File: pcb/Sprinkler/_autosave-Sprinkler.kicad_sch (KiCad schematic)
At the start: 6 parts, among them SW1 SW_Push_Open, U1 DHT11, U2 DS3231MZ

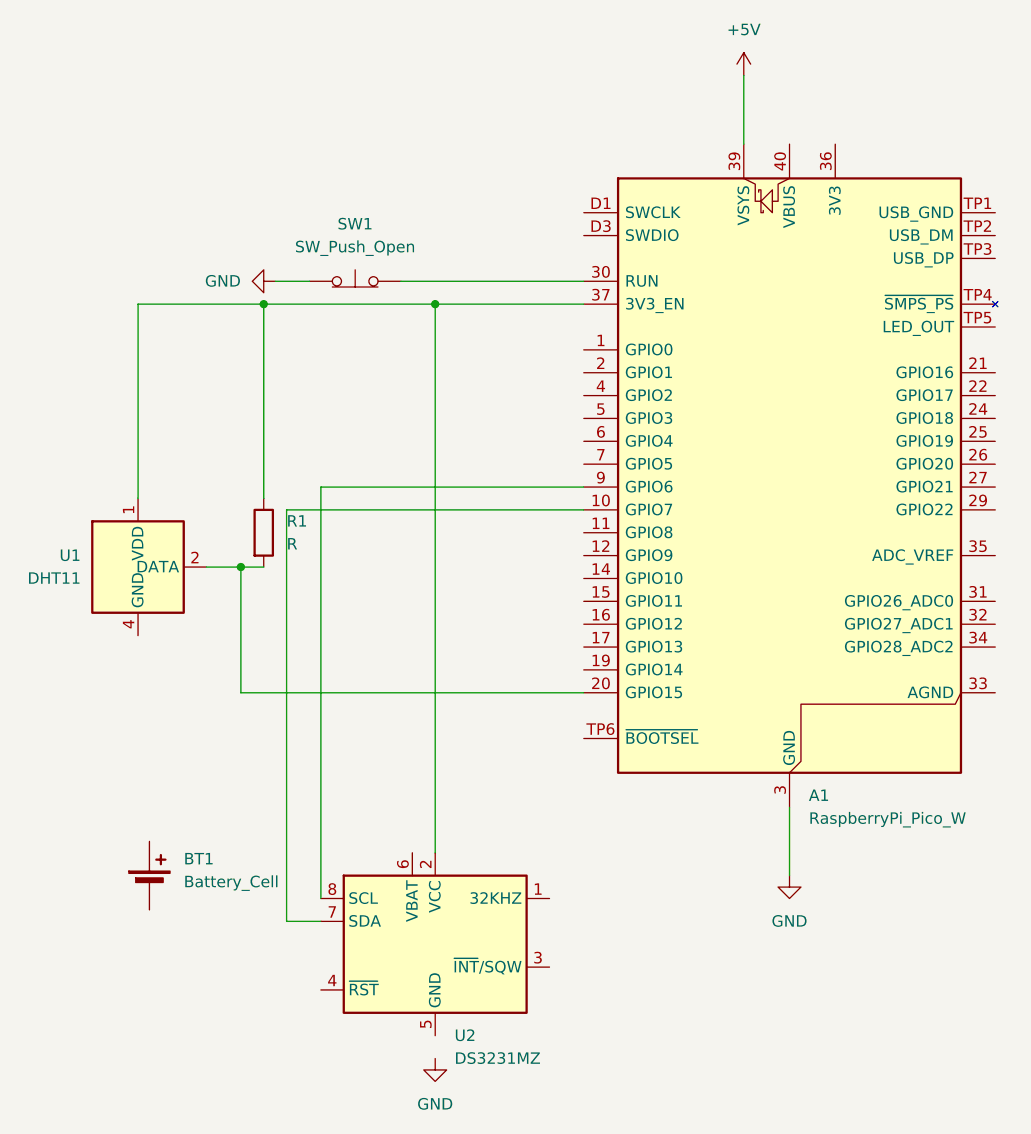
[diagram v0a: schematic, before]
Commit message: added alert and freeae protection
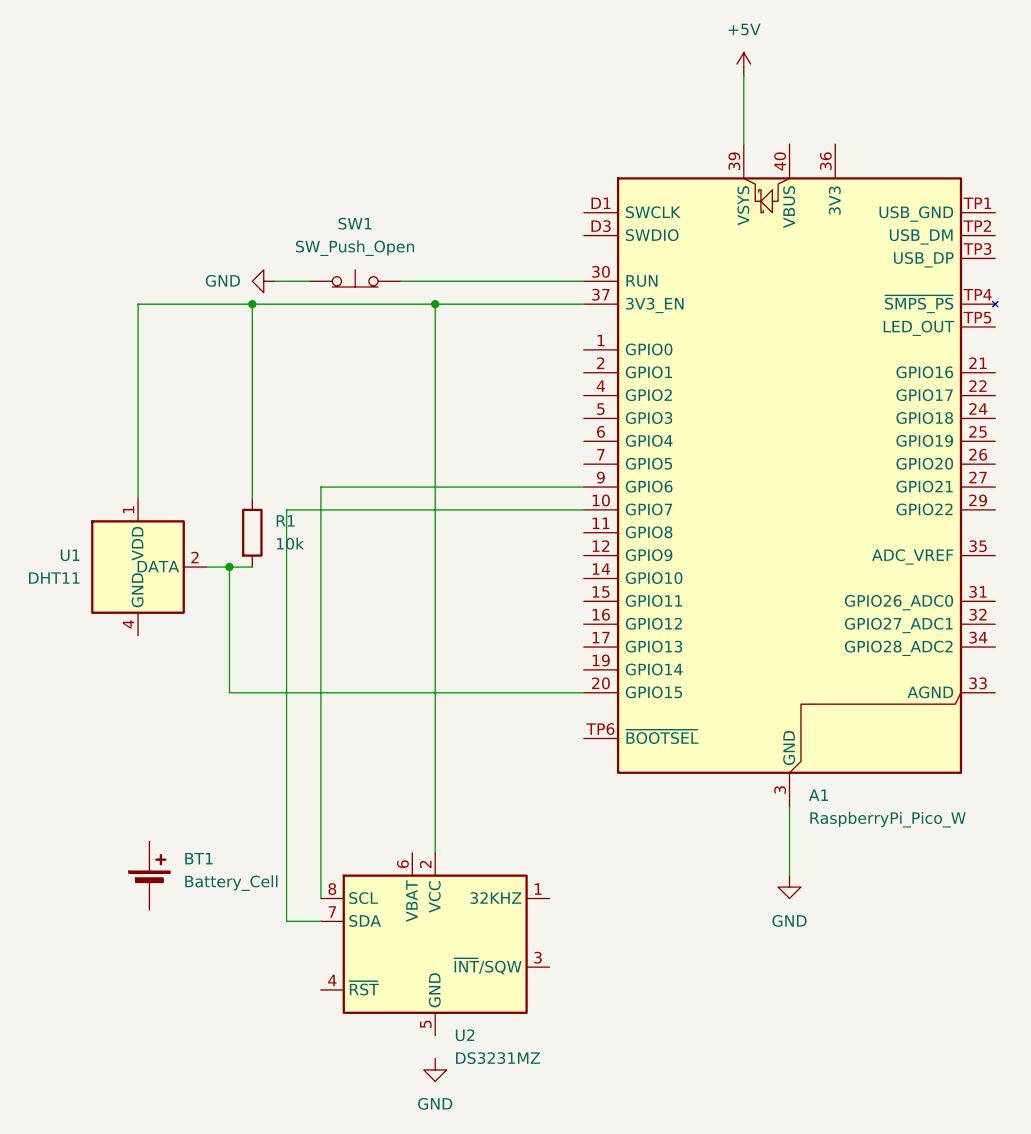
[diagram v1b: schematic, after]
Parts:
- R1: value R -> 10k
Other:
- moved on the sheet: R1
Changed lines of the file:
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@@
 	(paper "A4")
 	(junction
-		(at 76.2 83.82)
-		(diameter 0)
-		(color 0 0 0 0)
-	)
-	(junction
-		(at 78.74 54.61)
+		(at 74.93 83.82)
 		(diameter 0)
 		(color 0 0 0 0)
@@
 		(color 0 0 0 0)
 	)
-	(wire
-		(pts
-			(xy 78.74 54.61) (xy 97.79 54.61)
-		)
-		(stroke
-			(width 0)
-			(type default)
-		)
+	(junction
+		(at 77.47 54.61)
+		(diameter 0)
+		(color 0 0 0 0)
 	)
 	(wire
@@
 	(wire
 		(pts
-			(xy 76.2 83.82) (xy 78.74 83.82)
-		)
-		(stroke
-			(width 0)
-			(type default)
-		)
-	)
-	(wire
-		(pts
-			(xy 76.2 97.79) (xy 76.2 83.82)
+			(xy 74.93 83.82) (xy 77.47 83.82)
+		)
+		(stroke
+			(width 0)
+			(type default)
+		)
+	)
+	(wire
+		(pts
+			(xy 77.47 54.61) (xy 64.77 54.61)
+		)
+		(stroke
+			(width 0)
+			(type default)
+		)
+	)
+	(wire
+		(pts
+			(xy 74.93 97.79) (xy 74.93 83.82)
 		)
 		(stroke
@@
 	(wire
 		(pts
-			(xy 114.3 97.79) (xy 76.2 97.79)
+			(xy 114.3 97.79) (xy 74.93 97.79)
 		)
 		(stroke
@@
 	(wire
 		(pts
-			(xy 78.74 54.61) (xy 64.77 54.61)
+			(xy 77.47 54.61) (xy 97.79 54.61)
 		)
 		(stroke
@@
 	(wire
 		(pts
-			(xy 72.39 83.82) (xy 76.2 83.82)
+			(xy 72.39 83.82) (xy 74.93 83.82)
 		)
 		(stroke
@@
 	(wire
 		(pts
-			(xy 78.74 54.61) (xy 78.74 76.2)
+			(xy 77.47 54.61) (xy 77.47 76.2)
 		)
 		(stroke
@@
 	(symbol
 		(lib_id "Device:R")
-		(at 78.74 80.01 0)
+		(at 77.47 80.01 0)
 		(unit 1)
 		(exclude_from_sim no)
@@
 		(fields_autoplaced yes)
 		(property "Reference" "R1"
-			(at 81.28 78.7399 0)
+			(at 80.01 78.7399 0)
 			(effects
 				(font
@@
 			)
 		)
-		(property "Value" "R"
-			(at 81.28 81.2799 0)
+		(property "Value" "10k"
+			(at 80.01 81.2799 0)
 			(effects
 				(font
@@
 		)
 		(property "Footprint" ""
-			(at 76.962 80.01 90)
+			(at 75.692 80.01 90)
 			(effects
 				(font
@@
 		)
 		(property "Datasheet" "~"
-			(at 78.74 80.01 0)
+			(at 77.47 80.01 0)
 			(effects
 				(font
@@
 		)
 		(property "Description" "Resistor"
-			(at 78.74 80.01 0)
-			(effects
-				(font
+			(at 77.47 80.01 0)
+			(effects
+				(font
